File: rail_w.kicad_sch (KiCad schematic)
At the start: 54 parts

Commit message: PCBA prototype order
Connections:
- net +VLED: now also LED246.4 (VDD), LED247.4 (VDD), LED248.4 (VDD), LED249.4 (VDD)
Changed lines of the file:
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@@
 	)
 	(junction
+		(at 208.28 119.38)
+		(diameter 0)
+		(color 0 0 0 0)
+	)
+	(junction
 		(at 127 88.9)
 		(diameter 0)
@@
 	)
 	(junction
+		(at 167.64 119.38)
+		(diameter 0)
+		(color 0 0 0 0)
+	)
+	(junction
 		(at 181.61 39.37)
 		(diameter 0)
@@
 	)
 	(junction
+		(at 187.96 119.38)
+		(diameter 0)
+		(color 0 0 0 0)
+	)
+	(junction
 		(at 147.32 60.96)
 		(diameter 0)
@@
 	)
 	(junction
+		(at 147.32 119.38)
+		(diameter 0)
+		(color 0 0 0 0)
+	)
+	(junction
 		(at 45.72 60.96)
 		(diameter 0)
@@
 	(wire
 		(pts
+			(xy 187.96 119.38) (xy 187.96 129.54)
+		)
+		(stroke
+			(width 0)
+			(type default)
+		)
+	)
+	(wire
+		(pts
 			(xy 129.54 54.61) (xy 129.54 55.88)
 		)
@@
 	(wire
 		(pts
+			(xy 147.32 119.38) (xy 147.32 129.54)
+		)
+		(stroke
+			(width 0)
+			(type default)
+		)
+	)
+	(wire
+		(pts
 			(xy 209.55 81.28) (xy 210.82 81.28)
 		)
@@
 	(wire
 		(pts
+			(xy 147.32 119.38) (xy 167.64 119.38)
+		)
+		(stroke
+			(width 0)
+			(type default)
+		)
+	)
+	(wire
+		(pts
 			(xy 208.28 130.81) (xy 208.28 132.08)
 		)
@@
 	(wire
 		(pts
+			(xy 208.28 119.38) (xy 275.59 119.38)
+		)
+		(stroke
+			(width 0)
+			(type default)
+		)
+	)
+	(wire
+		(pts
 			(xy 63.5 154.94) (xy 64.77 154.94)
 		)
@@
 	(wire
 		(pts
+			(xy 167.64 119.38) (xy 167.64 129.54)
+		)
+		(stroke
+			(width 0)
+			(type default)
+		)
+	)
+	(wire
+		(pts
 			(xy 86.36 55.88) (xy 86.36 60.96)
 		)
@@
 	(wire
 		(pts
+			(xy 167.64 119.38) (xy 187.96 119.38)
+		)
+		(stroke
+			(width 0)
+			(type default)
+		)
+	)
+	(wire
+		(pts
 			(xy 45.72 60.96) (xy 66.04 60.96)
 		)
@@
 	(wire
 		(pts
+			(xy 208.28 119.38) (xy 208.28 129.54)
+		)
+		(stroke
+			(width 0)
+			(type default)
+		)
+	)
+	(wire
+		(pts
 			(xy 62.23 20.32) (xy 62.23 31.75)
 		)
@@
 	(wire
 		(pts
-			(xy 127 119.38) (xy 275.59 119.38)
+			(xy 127 119.38) (xy 147.32 119.38)
 		)
 		(stroke
@@
 		)
 		(stroke
+			(width 0)
+			(type default)
+		)
+	)
+	(wire
+		(pts
+			(xy 187.96 119.38) (xy 208.28 119.38)
+		)
+		(stroke

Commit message: Rev B component layout
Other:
- removed sheet Rail W Southbound

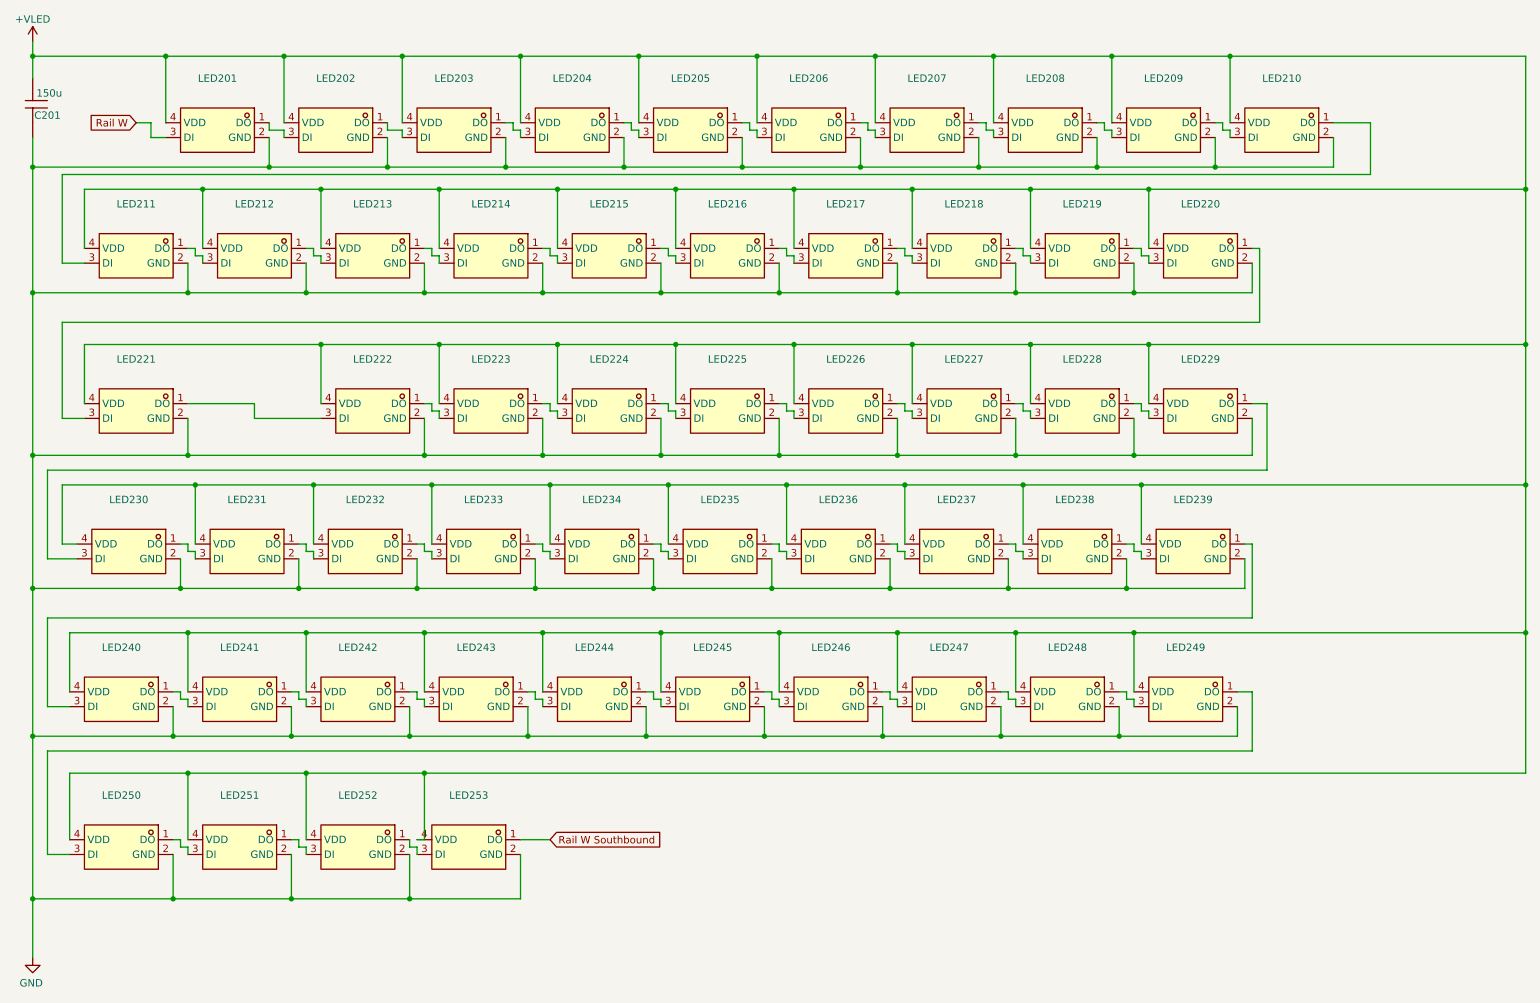
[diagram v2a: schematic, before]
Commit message: Add rail labels
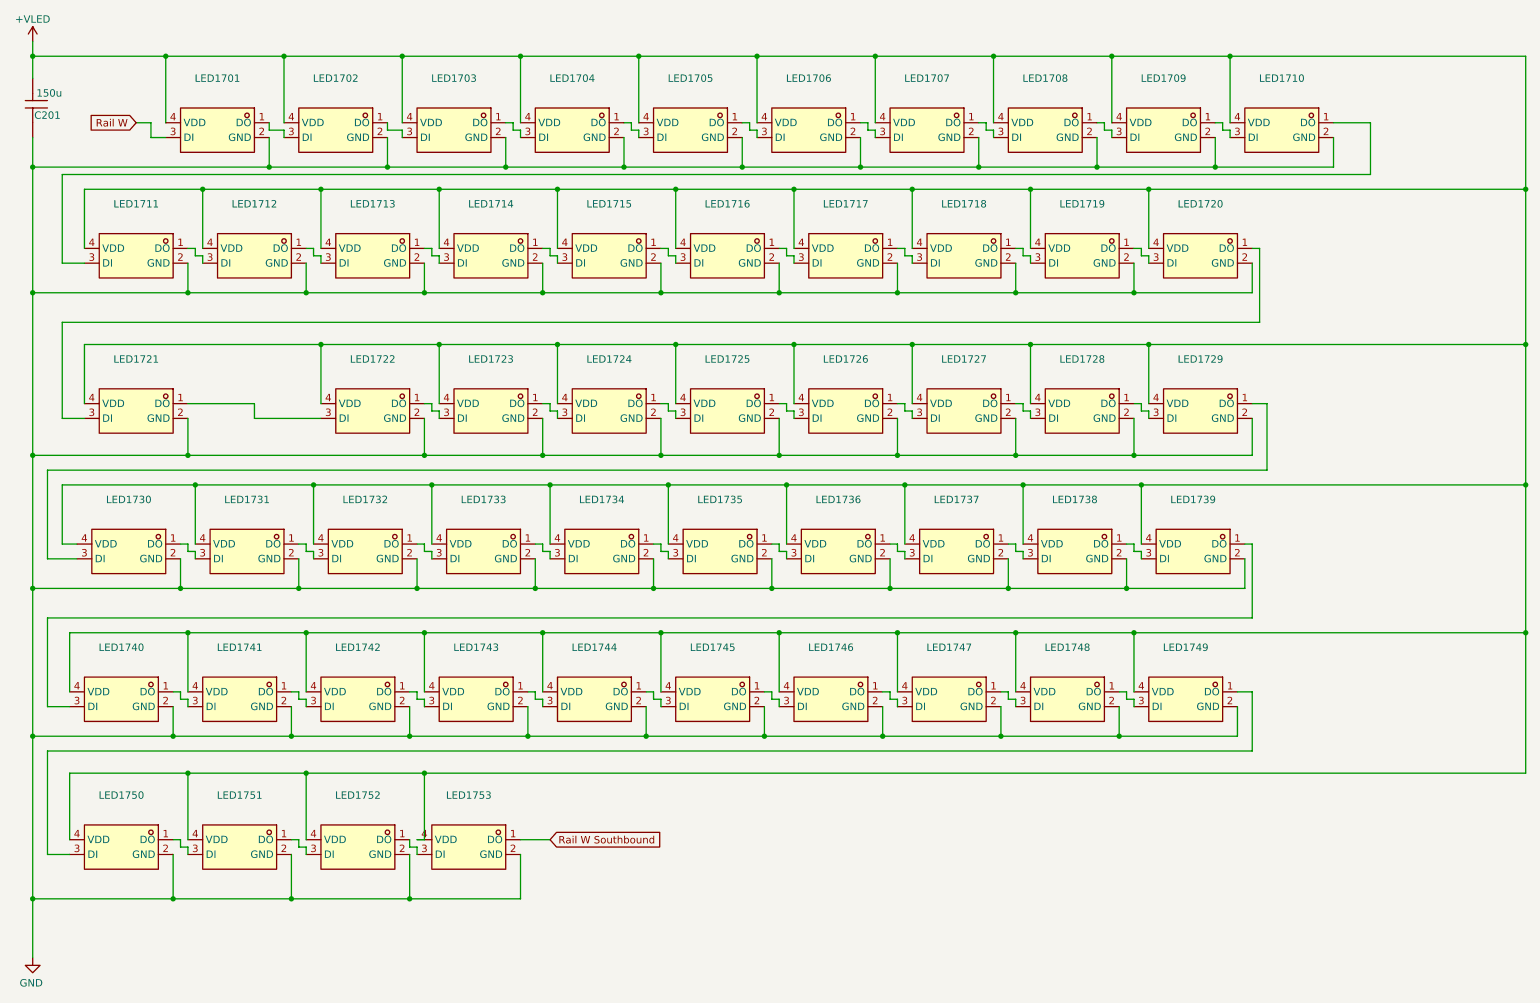
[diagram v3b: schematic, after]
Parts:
- renumbered LED201 to LED1701, LED202 to LED1702, LED203 to LED1703, LED204 to LED1704, LED205 to LED1705, LED206 to LED1706, LED207 to LED1707, LED208 to LED1708, LED209 to LED1709, LED210 to LED1710, LED211 to LED1711, LED212 to LED1712, LED213 to LED1713, LED214 to LED1714, LED215 to LED1715, LED216 to LED1716, LED217 to LED1717, LED218 to LED1718, LED219 to LED1719, LED220 to LED1720, LED221 to LED1721, LED222 to LED1722, LED223 to LED1723, LED224 to LED1724, LED225 to LED1725, LED226 to LED1726, LED227 to LED1727, LED228 to LED1728, LED229 to LED1729, LED230 to LED1730, LED231 to LED1731, LED232 to LED1732, LED233 to LED1733, LED234 to LED1734, LED235 to LED1735, LED236 to LED1736, LED237 to LED1737, LED238 to LED1738, LED239 to LED1739, LED240 to LED1740, LED241 to LED1741, LED242 to LED1742, LED243 to LED1743, LED244 to LED1744, LED245 to LED1745, LED246 to LED1746, LED247 to LED1747, LED248 to LED1748, LED249 to LED1749, LED250 to LED1750, LED251 to LED1751, LED252 to LED1752, LED253 to LED1753

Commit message: route T
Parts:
- renumbered LED1701 to LED1501, LED1702 to LED1502, LED1703 to LED1503, LED1704 to LED1504, LED1705 to LED1505, LED1706 to LED1506, LED1707 to LED1507, LED1708 to LED1508, LED1709 to LED1509, LED1710 to LED1510, LED1711 to LED1511, LED1712 to LED1512, LED1713 to LED1513, LED1714 to LED1514, LED1715 to LED1515, LED1716 to LED1516, LED1717 to LED1517, LED1718 to LED1518, LED1719 to LED1519, LED1720 to LED1520, LED1721 to LED1521, LED1722 to LED1522, LED1723 to LED1523, LED1724 to LED1524, LED1725 to LED1525, LED1726 to LED1526, LED1727 to LED1527, LED1728 to LED1528, LED1729 to LED1529, LED1730 to LED1530, LED1731 to LED1531, LED1732 to LED1532, LED1733 to LED1533, LED1734 to LED1534, LED1735 to LED1535, LED1736 to LED1536, LED1737 to LED1537, LED1738 to LED1538, LED1739 to LED1539, LED1740 to LED1540, LED1741 to LED1541, LED1742 to LED1542, LED1743 to LED1543, LED1744 to LED1544, LED1745 to LED1545, LED1746 to LED1546, LED1747 to LED1547, LED1748 to LED1548, LED1749 to LED1549, LED1750 to LED1550, LED1751 to LED1551, LED1752 to LED1552, LED1753 to LED1553

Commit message: route link 1
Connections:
- net Rail W renamed LINK_1_N
- net Rail W Southbound renamed LINK_1_S
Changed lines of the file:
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@@
 		)
 	)
-	(global_label "Rail W"
+	(global_label "LINK_1_N"
 		(shape input)
 		(at 36.83 31.75 180)
@@
 		)
 		(property "Intersheetrefs" "${INTERSHEET_REFS}"
-			(at 27.7368 31.75 0)
+			(at 25.1362 31.75 0)
 			(hide yes)
 			(show_name no)
@@
 		)
 	)
-	(global_label "Rail W Southbound"
+	(global_label "LINK_1_S"
 		(shape input)
 		(at 107.95 154.94 0)
@@
 		)
 		(property "Intersheetrefs" "${INTERSHEET_REFS}"
-			(at 129.138 154.94 0)
+			(at 119.5228 154.94 0)
 			(hide yes)
 			(show_name no)

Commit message: rev-b validation run
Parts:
- removed C201: 150u, EasyEDA:CAP-SMD_L3.5-W2.8, symbol EasyEDA:CL21B106KOQNNNE
- LED1501, LED1502, LED1503, LED1504, LED1505, LED1506, LED1507, LED1508, LED1509, LED1510, LED1511, LED1512, LED1513, LED1514, LED1515, LED1516, LED1517, LED1518, LED1519, LED1520, LED1521, LED1522, LED1523, LED1524, LED1525, LED1526, LED1527, LED1528, LED1529, LED1530, LED1531, LED1532, LED1533, LED1534, LED1535, LED1536, LED1537, LED1538, LED1539, LED1540, LED1541, LED1542, LED1543, LED1544, LED1545, LED1546, LED1547, LED1548, LED1549, LED1550, LED1551, LED1552, LED1553: LCSC Part C965555 -> C52917434
